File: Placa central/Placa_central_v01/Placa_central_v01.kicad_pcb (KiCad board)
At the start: 2 copper layers, 68 parts, among them J1 PinoCheckBateriaVcc, J10 Conn_01x01_Arduino11, J11 Conn_01x01_Arduino12, J12 Conn_01x01_Arduino13, J13 Conn_01x01_Arduino14, J14 Conn_01x01_Arduino15, J15 Conn_01x01_Arduino16, J16 Conn_01x01_Motor1PonteHPCB, J17 PinoCheckBateriaGND, J18 Conn_01x01_Arduino19, J19 Conn_01x01_Arduino20, J2 Conn_01x02_ArduinoTxRx, J20 Conn_01x01_Arduino21, J21 Conn_01x01_Arduino22, J22 Conn_01x01_Arduino23, J23 Conn_01x01_Arduino24, J24 Conn_01x01_Arduino25, J25 Conn_01x01_Arduino26, J26 Conn_02x08_Odd_Even, J27 Conn_01x01_Motor2PonteHPCB, J28 Conn_01x01_Motor1PCBMotor, J29 Conn_01x01_Motor2PCBMotor, J3 Conn_01x01_ArduinoReset, J37 Conn_01x01_8.4VPonteH, J38 Conn_01x01_5VPonteH, J39 Conn_01x01_GNDPonteH, J4 Conn_01x01_Arduino5, J40 Conn_01x01_Motor1PWM, J41 Conn_01x01_Motor1Dir1, J42 Conn_01x01_Motor1Dir2, J43 Conn_01x01_Motor2Dir1, J44 Conn_01x01_Motor2Dir2, J45 Conn_01x01_Motor2PWM, J48 Conn_01x01_5VEncoderEsq, J49 Conn_01x01_OutputEncoderEsq, J5 Conn_01x01_Arduino6, J50 Conn_01x01_GNDEncoderEsq, J51 Conn_01x01_5VEncoderDir, J52 Conn_01x01_OutputEncoderDir, J53 Conn_01x01_GNDEncoderDir, J6 Conn_01x01_Arduino7, J7 Conn_01x01_Arduino8, J8 Conn_01x01_Arduino9, J9 Conn_01x01_Arduino10, Q1 BC548, Q2 BC548, SW1 SW_ON/OFF, SW3 SW_comando1

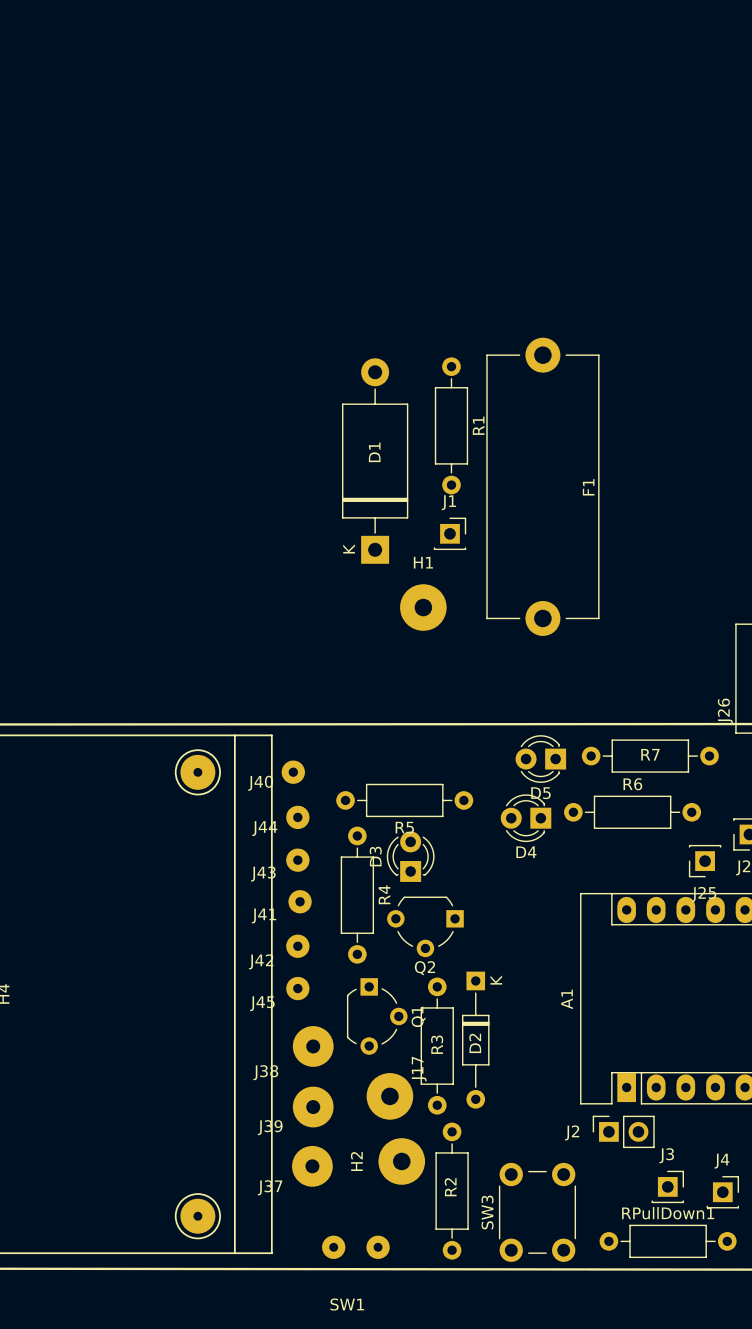
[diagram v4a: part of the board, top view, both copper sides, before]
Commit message: Placa auxiliar de alimentacao rooteada, placa central AINDA DESATUALIZADA
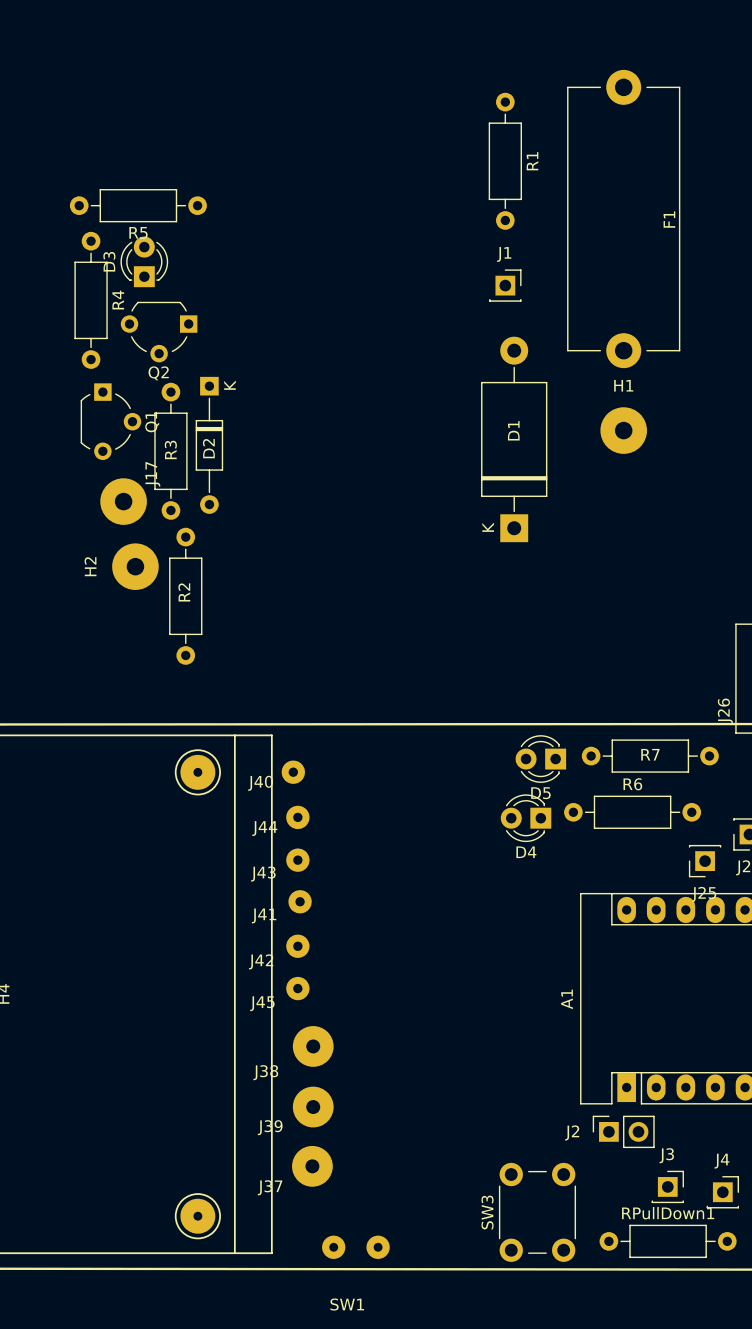
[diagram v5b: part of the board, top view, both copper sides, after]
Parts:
- moved Q1 55.9 mm to (73.4, 95.0)
- moved R2 55.9 mm to (80.5, 107.4)
- moved R3 55.9 mm to (79.2, 95.0)
- moved D2 55.9 mm to (82.5, 94.5)
- moved D3 55.9 mm to (77.0, 85.1)
- moved H2 55.9 mm to (76.2, 110.0)
- moved J17 55.9 mm to (75.2, 104.4)
- moved Q2 55.9 mm to (80.8, 89.2)
- moved R4 55.9 mm to (72.4, 82.0)
- moved R5 55.9 mm to (81.5, 79.0)
- moved F1 24.0 mm to (118.1, 91.4)
- moved R1 23.2 mm to (108.0, 70.1)
- moved H1 22.9 mm to (118.1, 98.3)
- moved J1 21.8 mm to (108.0, 85.9)
- moved D1 12.1 mm to (108.7, 106.7)
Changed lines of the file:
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@@
   )
   (module Diode_THT:D_DO-35_SOD27_P10.16mm_Horizontal (layer F.Cu)
-    (at 105.41 145.542 270)
+    (at 82.55 94.488 270)
     (descr "Diode, DO-35_SOD27 series, Axial, Horizontal, pin pitch=10.16mm, , length*diameter=4*2mm^2, , http://www.diodes.com/_files/packages/DO-35.pdf")
     (tags "Diode DO-35_SOD27 series Axial Horizontal pin pitch 10.16mm  length 4mm diameter 2mm")
@@
   )
   (module Resistor_THT:R_Axial_DIN0207_L6.3mm_D2.5mm_P10.16mm_Horizontal (layer F.Cu)
-    (at 103.378 158.496 270)
+    (at 80.518 107.442 270)
     (descr "Resistor, Axial_DIN0207 series, Axial, Horizontal, pin pitch=10.16mm, 0.25W = 1/4W, length*diameter=6.3*2.5mm^2, http://cdn-reichelt.de/documents/datenblatt/B400/1_4W%23YAG.pdf")
     (tags "Resistor Axial_DIN0207 series Axial Horizontal pin pitch 10.16mm 0.25W = 1/4W length 6.3mm diameter 2.5mm")
@@
   )
   (module LED_THT:LED_D3.0mm (layer F.Cu)
-    (at 99.822 136.144 90)
+    (at 76.962 85.09 90)
     (descr "LED, diameter 3.0mm, 2 pins")
     (tags "LED diameter 3.0mm 2 pins")
@@
   )
   (module Resistor_THT:R_Axial_DIN0207_L6.3mm_D2.5mm_P10.16mm_Horizontal (layer F.Cu)
-    (at 95.25 133.096 270)
+    (at 72.39 82.042 270)
     (descr "Resistor, Axial_DIN0207 series, Axial, Horizontal, pin pitch=10.16mm, 0.25W = 1/4W, length*diameter=6.3*2.5mm^2, http://cdn-reichelt.de/documents/datenblatt/B400/1_4W%23YAG.pdf")
     (tags "Resistor Axial_DIN0207 series Axial Horizontal pin pitch 10.16mm 0.25W = 1/4W length 6.3mm diameter 2.5mm")
@@
   )
   (module Package_TO_SOT_THT:TO-92_Wide (layer F.Cu)
-    (at 103.632 140.208 180)
+    (at 80.772 89.154 180)
     (descr "TO-92 leads molded, wide, drill 0.75mm (see NXP sot054_po.pdf)")
     (tags "to-92 sc-43 sc-43a sot54 PA33 transistor")
@@
   )
   (module Diode_THT:D_DO-27_P15.24mm_Horizontal (layer F.Cu)
-    (at 96.774 108.5342 90)
+    (at 108.712 106.68 90)
     (descr "Diode, DO-27 series, Axial, Horizontal, pin pitch=15.24mm, , length*diameter=9.52*5.33mm^2, , http://www.slottechforum.com/slotinfo/Techstuff/CD2%20Diodes%20and%20Transistors/Cases/Diode%20DO-27.jpg")
     (tags "Diode DO-27 series Axial Horizontal pin pitch 15.24mm  length 9.52mm diameter 5.33mm")
@@
   )
   (module Fuse:Fuseholder_Cylinder-5x20mm_Stelvio-Kontek_PTF78_Horizontal_Open (layer F.Cu)
-    (at 111.1758 114.427 90)
+    (at 118.11 91.44 90)
     (descr https://www.tme.eu/en/Document/3b48dbe2b9714a62652c97b08fcd464b/PTF78.pdf)
     (tags "Fuseholder horizontal open 5x20 Stelvio-Kontek PTF/78")
@@
   )
   (module Connector_Wire:SolderWirePad_1x01_Drill1.5mm (layer F.Cu)
-    (at 100.9142 113.4872)
+    (at 118.11 98.298)
     (descr "Wire solder connection")
     (tags connector)
@@
   )
   (module Connector_Wire:SolderWirePad_1x01_Drill1.5mm (layer F.Cu)
-    (at 99.06 161.036 90)
+    (at 76.2 109.982 90)
     (descr "Wire solder connection")
     (tags connector)
@@
   )
   (module Connector_PinSocket_2.54mm:PinSocket_1x01_P2.54mm_Vertical (layer F.Cu)
-    (at 103.2002 107.1626)
+    (at 107.95 85.852)
     (descr "Through hole straight socket strip, 1x01, 2.54mm pitch, single row (from Kicad 4.0.7), script generated")
     (tags "Through hole socket strip THT 1x01 2.54mm single row")
@@
   )
   (module Package_TO_SOT_THT:TO-92_Wide (layer F.Cu)
-    (at 96.266 146.05 270)
+    (at 73.406 94.996 270)
     (descr "TO-92 leads molded, wide, drill 0.75mm (see NXP sot054_po.pdf)")
     (tags "to-92 sc-43 sc-43a sot54 PA33 transistor")
@@
   )
   (module Resistor_THT:R_Axial_DIN0207_L6.3mm_D2.5mm_P10.16mm_Horizontal (layer F.Cu)
-    (at 103.3272 92.8116 270)
+    (at 107.95 70.104 270)
     (descr "Resistor, Axial_DIN0207 series, Axial, Horizontal, pin pitch=10.16mm, 0.25W = 1/4W, length*diameter=6.3*2.5mm^2, http://cdn-reichelt.de/documents/datenblatt/B400/1_4W%23YAG.pdf")
     (tags "Resistor Axial_DIN0207 series Axial Horizontal pin pitch 10.16mm 0.25W = 1/4W length 6.3mm diameter 2.5mm")
@@
   )
   (module Resistor_THT:R_Axial_DIN0207_L6.3mm_D2.5mm_P10.16mm_Horizontal (layer F.Cu)
-    (at 102.108 146.05 270)
+    (at 79.248 94.996 270)
     (descr "Resistor, Axial_DIN0207 series, Axial, Horizontal, pin pitch=10.16mm, 0.25W = 1/4W, length*diameter=6.3*2.5mm^2, http://cdn-reichelt.de/documents/datenblatt/B400/1_4W%23YAG.pdf")
     (tags "Resistor Axial_DIN0207 series Axial Horizontal pin pitch 10.16mm 0.25W = 1/4W length 6.3mm diameter 2.5mm")
@@
   )
   (module Resistor_THT:R_Axial_DIN0207_L6.3mm_D2.5mm_P10.16mm_Horizontal (layer F.Cu)
-    (at 104.394 130.048 180)
+    (at 81.534 78.994 180)
     (descr "Resistor, Axial_DIN0207 series, Axial, Horizontal, pin pitch=10.16mm, 0.25W = 1/4W, length*diameter=6.3*2.5mm^2, http://cdn-reichelt.de/documents/datenblatt/B400/1_4W%23YAG.pdf")
     (tags "Resistor Axial_DIN0207 series Axial Horizontal pin pitch 10.16mm 0.25W = 1/4W length 6.3mm diameter 2.5mm")
@@
   )
   (module Connector_Wire:SolderWirePad_1x01_Drill1.5mm (layer F.Cu)
-    (at 98.044 155.448 90)
+    (at 75.184 104.394 90)
     (descr "Wire solder connection")
     (tags connector)

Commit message: Distribuição dos compenentes praticamente concluída, quase pronta para root.
Placa Central: 5VArduino(pino 15) colocado no pino 16, enquanto o sensorEsq(pino 16) foi colocado no pino 15 para
facilitar o root; Adicionado na placa central os pads de conexao das alimentacoes provenientes do circuito de
alimentacao; Label '5V' substituída por '5VArduino' - decisão a ser revisada; Pads de solda trocados por pads maiores
por questoes de corrente alta (pinos de alimentacao). *Placa de Alimentação: Nome de dois pinos da placa de alimentação
modificados. Pads de solda trocados por pads maiores por questoes de corrente alta (pinos de alimentacao).
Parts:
- removed D1: DiodoProtecao-5A, Diode_THT:D_DO-27_P15.24mm_Horizontal
- removed D2: DiodoZener6.8V, Diode_THT:D_DO-35_SOD27_P10.16mm_Horizontal
- removed D3: LedBateriaVermelho, LED_THT:LED_D3.0mm
- removed F1: Fuse-5A, Fuse:Fuseholder_Cylinder-5x20mm_Stelvio-Kontek_PTF78_Horizontal_Open
- removed H1: V8.4 - Lipo, Connector_Wire:SolderWirePad_1x01_Drill1.5mm
- removed H2: GND - Lipo, Connector_Wire:SolderWirePad_1x01_Drill1.5mm
- removed J10: Conn_01x01_Arduino11, Connector_PinSocket_2.54mm:PinSocket_1x01_P2.54mm_Vertical
- removed J11: Conn_01x01_Arduino12, Connector_PinSocket_2.54mm:PinSocket_1x01_P2.54mm_Vertical
- removed J12: Conn_01x01_Arduino13, Connector_PinSocket_2.54mm:PinSocket_1x01_P2.54mm_Vertical
- removed J13: Conn_01x01_Arduino14, Connector_PinSocket_2.54mm:PinSocket_1x01_P2.54mm_Vertical
- removed J14: Conn_01x01_Arduino15, Connector_PinSocket_2.54mm:PinSocket_1x01_P2.54mm_Vertical
- removed J15: Conn_01x01_Arduino16, Connector_PinSocket_2.54mm:PinSocket_1x01_P2.54mm_Vertical
- removed J17: PinoCheckBateriaGND, Connector_Wire:SolderWirePad_1x01_Drill1.5mm
- removed J18: Conn_01x01_Arduino19, Connector_PinSocket_2.54mm:PinSocket_1x01_P2.54mm_Vertical
- removed J19: Conn_01x01_Arduino20, Connector_PinSocket_2.54mm:PinSocket_1x01_P2.54mm_Vertical
- removed J20: Conn_01x01_Arduino21, Connector_PinSocket_2.54mm:PinSocket_1x01_P2.54mm_Vertical
- removed J21: Conn_01x01_Arduino22, Connector_PinSocket_2.54mm:PinSocket_1x01_P2.54mm_Vertical
- removed J22: Conn_01x01_Arduino23, Connector_PinSocket_2.54mm:PinSocket_1x01_P2.54mm_Vertical
- removed J23: Conn_01x01_Arduino24, Connector_PinSocket_2.54mm:PinSocket_1x01_P2.54mm_Vertical
- removed J24: Conn_01x01_Arduino25, Connector_PinSocket_2.54mm:PinSocket_1x01_P2.54mm_Vertical
- removed J25: Conn_01x01_Arduino26, Connector_PinSocket_2.54mm:PinSocket_1x01_P2.54mm_Vertical
- removed J5: Conn_01x01_Arduino6, Connector_PinSocket_2.54mm:PinSocket_1x01_P2.54mm_Vertical
- removed J6: Conn_01x01_Arduino7, Connector_PinSocket_2.54mm:PinSocket_1x01_P2.54mm_Vertical
- removed J7: Conn_01x01_Arduino8, Connector_PinSocket_2.54mm:PinSocket_1x01_P2.54mm_Vertical
- removed J8: Conn_01x01_Arduino9, Connector_PinSocket_2.54mm:PinSocket_1x01_P2.54mm_Vertical
- removed J9: Conn_01x01_Arduino10, Connector_PinSocket_2.54mm:PinSocket_1x01_P2.54mm_Vertical
- removed Q1, Q2: BC548, Package_TO_SOT_THT:TO-92_Wide
- removed R1: RBatCheck10K, Resistor_THT:R_Axial_DIN0207_L6.3mm_D2.5mm_P10.16mm_Horizontal
- removed R2: R6K6MedidorDeBateria, Resistor_THT:R_Axial_DIN0207_L6.3mm_D2.5mm_P10.16mm_Horizontal
- removed R3: R1KMedidorDeBateria, Resistor_THT:R_Axial_DIN0207_L6.3mm_D2.5mm_P10.16mm_Horizontal
- removed R4: R10KMedidorDeBateria, Resistor_THT:R_Axial_DIN0207_L6.3mm_D2.5mm_P10.16mm_Horizontal
- removed R5: RMedidorDeBateria1K, Resistor_THT:R_Axial_DIN0207_L6.3mm_D2.5mm_P10.16mm_Horizontal
- removed SW1: SW_ON/OFF, CUSTOM_Placa_central_v01:Solder_Pad_Custom
- J1: value PinoCheckBateriaVcc -> Conn_8.4V_PlacaAlimentação; footprint Connector_PinSocket_2.54mm:PinSocket_1x01_P2.54mm_Vertical -> Connector_Wire:SolderWirePad_1x01_Drill1.2mm
- J4: value Conn_01x01_Arduino5 -> Conn_GND_PlacaAlimentação; footprint Connector_PinSocket_2.54mm:PinSocket_1x01_P2.54mm_Vertical -> Connector_Wire:SolderWirePad_1x01_Drill1.2mm
- moved J16 178.1 mm to (96.5, 107.7)
- moved J28 178.1 mm to (58.9, 108.2)
- moved F3 178.1 mm to (60.0, 82.2)
- moved J27 178.1 mm to (42.2, 84.3)
- moved F2 178.1 mm to (88.3, 108.2)
- moved J29 178.1 mm to (104.2, 83.8)
- moved J1 41.9 mm to (103.6, 127.5)
- moved J4 38.7 mm to (111.5, 128.0)
- moved J51 34.1 mm to (159.5, 133.6)
- moved J48 28.2 mm to (34.8, 134.9)
- moved D4 16.0 mm to (112.0, 147.6)
- moved D5 15.0 mm to (106.9, 140.5), turned to 270 degrees
- moved J53 14.7 mm to (146.6, 165.4)
- moved R6 12.5 mm to (113.3, 143.5), turned to 90 degrees
- moved J50 12.2 mm to (36.6, 159.3)
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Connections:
- net ArduinD6 renamed Net-(A1-Pad9)
- J1 pad 1: Net-(J1-Pad1) -> 8.4V
- J26 pad 15: 5VArduino -> SensorEsq
- J26 pad 16: SensorEsq -> 5VArduino
- J4 pad 1: Encoder1 -> GND
- SW3 pad 1: 5V -> 5VArduino

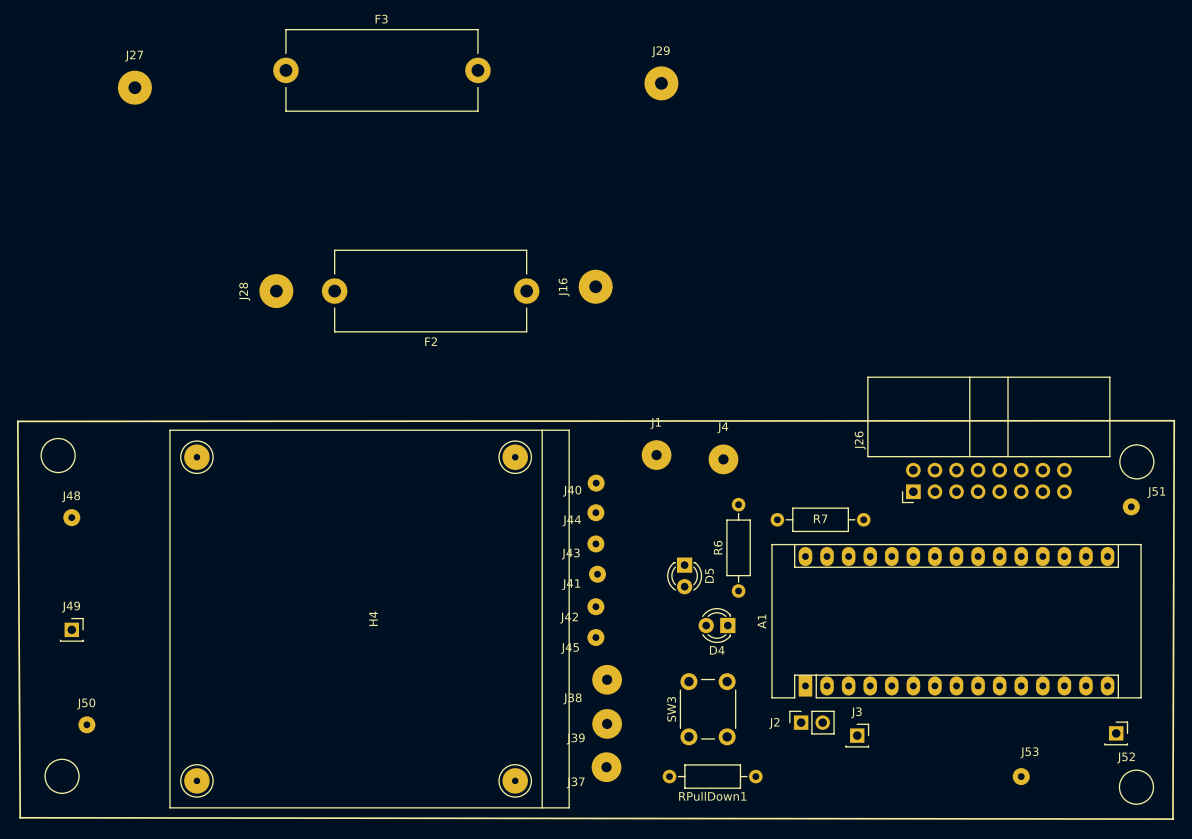
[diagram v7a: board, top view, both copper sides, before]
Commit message: Root finalizado, aguardando revisão dos demais membros. Ocorreram mudanças massivas nas conexões de pinos lógicos e do conector.
Track Width (grossura da linha) modificado para 0,9 mm na placa central. Conexões do Conector rearranjadas.
Tag 'Botão1' movida para o pino 6;
Tag 'Arduino13' (agora vago - pino 16) adicionado ao conector;
Pino ArduinoD13 será adicionado ao conector (se possível), para possível uso futuro. Outros pinos extras não serão adicionados. O pino será de fato adicionado na PBC dos sensores.
Tag 'Motor1Pwm' movida para o pino 13;
Tag 'Motor2Dir2' movida para o pino 12;
Tag 'Motor2Dir1' movida para pino 11;
Tag 'Motor1Dir1' movida para o pino 10;
Tag 'Encoder2' movida para o pino 7;
Tag 'Motor2PWM' movida para o pino 8;
Tag 'Motor1Dir2' movida para o pino 9;
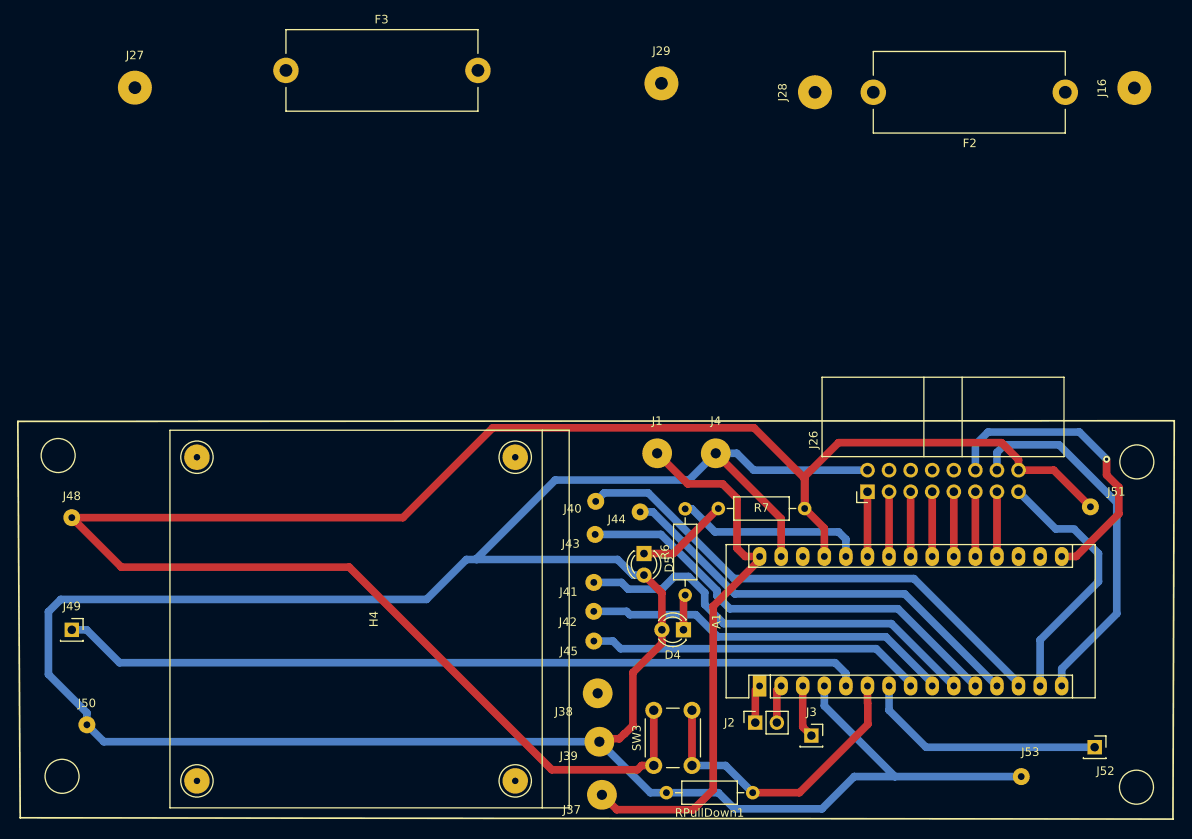
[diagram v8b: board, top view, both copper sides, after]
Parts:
- moved J16 67.6 mm to (159.9, 84.3)
- moved F2 67.6 mm to (151.7, 84.8)
- moved J28 67.6 mm to (122.3, 84.8)
- moved R7 7.08 mm to (110.9, 133.8)
- moved R6 6.30 mm to (107.0, 144.0)
- moved A1 5.40 mm to (115.8, 154.7)
- moved J2 5.40 mm to (115.2, 159.0)
- moved J26 5.40 mm to (128.5, 131.8)
- moved J3 5.40 mm to (121.9, 160.5)
- moved SW3 5.34 mm to (103.3, 164.1)
- moved D4 5.24 mm to (106.8, 148.1)
- moved J44 5.21 mm to (101.7, 134.2)
- moved D5 4.97 mm to (102.2, 139.1)
- moved J51 4.81 mm to (154.7, 133.6)
- moved J37 3.30 mm to (97.2, 167.5)
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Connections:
- A1 pad 10: Motor2PWM -> Motor1Dir1
- A1 pad 11: Motor1PWM -> Motor2Dir1
- A1 pad 12: Motor2Dir1 -> Motor2Dir2
- A1 pad 13: Motor2Dir2 -> Motor1PWM
- A1 pad 16: Botao1 -> ArduinoD13
- A1 pad 6: Encoder2 -> Botao1
- A1 pad 7: Motor1Dir1 -> Encoder2
- A1 pad 8: Motor1Dir2 -> Motor2PWM
- A1 pad 9: Net-(A1-Pad9) -> Motor1Dir2
- J26 pad 1: GND -> Sensor7
- J26 pad 12: Sensor7 -> ArduinoD13
- J26 pad 14: Net-(J26-Pad14) -> SensorDir
- J26 pad 2: SensorDir -> GND
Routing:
- net GND: track 0.00 -> 310.5 mm
- net 5VArduino: track 0.00 -> 233.7 mm
- net Encoder1: track 0.00 -> 94.7 mm
- net 8.4V: track 0.00 -> 65.1 mm
- net Motor1PWM: track 0.00 -> 59.8 mm
- net Motor2Dir1: track 0.00 -> 52.5 mm
- net Motor2Dir2: track 0.00 -> 50.5 mm
- net Motor1Dir1: track 0.00 -> 49.8 mm
- net Motor1Dir2: track 0.00 -> 43.7 mm
- net SensorDir: track 0.00 -> 43.6 mm
- net Motor2PWM: track 0.00 -> 39.7 mm
- net Botao1: track 0.00 -> 36.7 mm
- net ArduinoD13: track 0.00 -> 36.2 mm, vias 0 -> 1
- net SensorEsq: track 0.00 -> 30.7 mm
- net Encoder2: track 0.00 -> 28.9 mm
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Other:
- net class Default: clearance 0.2 -> 0.3; trace_width 0.25 -> 0.9
- rule trace_clearance: 0.2 -> 0.3
